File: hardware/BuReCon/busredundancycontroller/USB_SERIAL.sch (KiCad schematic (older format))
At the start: 27 parts, among them U4 FT2232HL, U5 USBLC6-2SC6, U6 93LC56C, U7 DSC1001DI1

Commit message: House Keeping
House keeping
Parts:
- C13, C14, C15, C16, C17, C18, C19, C20, C21, C22, C23, C24, C25, C26, C27: footprint (none) -> Capacitor_SMD:C_0201_0603Metric
- FB2, FB3: footprint (none) -> Fuse:Fuse_0603_1608Metric
- R2, R3, R4, R5, R6, R7: footprint (none) -> Resistor_SMD:R_0603_1608Metric
- U6: footprint (none) -> Package_TO_SOT_SMD:SOT-23-8
- U7: footprint CDFN4_2P5X2_MCH -> CDFN4_2P5X2_MCH:DSC1001DI1-033.3333T
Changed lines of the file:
@@
 F 0 "C16" H 9042 1846 50  0000 L CNN
 F 1 "100nF" H 9042 1755 50  0000 L CNN
-F 2 "" H 8950 1800 50  0001 C CNN
+F 2 "Capacitor_SMD:C_0201_0603Metric" H 8950 1800 50  0001 C CNN
 F 3 "~" H 8950 1800 50  0001 C CNN
 	1    8950 1800
@@
 F 0 "C17" H 9442 1846 50  0000 L CNN
 F 1 "100nF" H 9442 1755 50  0000 L CNN
-F 2 "" H 9350 1800 50  0001 C CNN
+F 2 "Capacitor_SMD:C_0201_0603Metric" H 9350 1800 50  0001 C CNN
 F 3 "~" H 9350 1800 50  0001 C CNN
 	1    9350 1800
@@
 F 0 "C18" H 9842 1846 50  0000 L CNN
 F 1 "100nF" H 9842 1755 50  0000 L CNN
-F 2 "" H 9750 1800 50  0001 C CNN
+F 2 "Capacitor_SMD:C_0201_0603Metric" H 9750 1800 50  0001 C CNN
 F 3 "~" H 9750 1800 50  0001 C CNN
 	1    9750 1800
@@
 F 0 "C15" H 8642 1846 50  0000 L CNN
 F 1 "100nF" H 8642 1755 50  0000 L CNN
-F 2 "" H 8550 1800 50  0001 C CNN
+F 2 "Capacitor_SMD:C_0201_0603Metric" H 8550 1800 50  0001 C CNN
 F 3 "~" H 8550 1800 50  0001 C CNN
 	1    8550 1800
@@
 F 0 "FB2" V 4400 950 50  0000 C CNN
 F 1 "BLM18SG121TN1D" V 4700 900 50  0000 C CNN
-F 2 "" V 4480 950 50  0001 C CNN
+F 2 "Fuse:Fuse_0603_1608Metric" V 4480 950 50  0001 C CNN
 F 3 "https://datasheet.octopart.com/BLM18SG121TN1D-Murata-datasheet-138707216.pdf" H 4550 950 50  0001 C CNN
 	1    4550 950
@@
 F 0 "FB3" V 3900 1650 50  0000 C CNN
 F 1 "BLM18SG121TN1D" V 4200 1450 50  0000 C CNN
-F 2 "" V 3980 1650 50  0001 C CNN
+F 2 "Fuse:Fuse_0603_1608Metric" V 3980 1650 50  0001 C CNN
 F 3 "https://datasheet.octopart.com/BLM18SG121TN1D-Murata-datasheet-138707216.pdf" H 4050 1650 50  0001 C CNN
 	1    4050 1650
@@
 F 0 "C13" H 5092 1146 50  0000 L CNN
 F 1 "10nF" H 5092 1055 50  0000 L CNN
-F 2 "" H 5000 1100 50  0001 C CNN
+F 2 "Capacitor_SMD:C_0201_0603Metric" H 5000 1100 50  0001 C CNN
 F 3 "~" H 5000 1100 50  0001 C CNN
 	1    5000 1100
@@
 F 0 "C14" H 5492 1146 50  0000 L CNN
 F 1 "100nF" H 5492 1055 50  0000 L CNN
-F 2 "" H 5400 1100 50  0001 C CNN
+F 2 "Capacitor_SMD:C_0201_0603Metric" H 5400 1100 50  0001 C CNN
 F 3 "~" H 5400 1100 50  0001 C CNN
 	1    5400 1100
@@
 F 0 "C19" H 4392 1796 50  0000 L CNN
 F 1 "10nF" H 4392 1705 50  0000 L CNN
-F 2 "" H 4300 1750 50  0001 C CNN
+F 2 "Capacitor_SMD:C_0201_0603Metric" H 4300 1750 50  0001 C CNN
 F 3 "~" H 4300 1750 50  0001 C CNN
 	1    4300 1750
@@
 F 0 "C20" H 4842 1796 50  0000 L CNN
 F 1 "100nF" H 4842 1705 50  0000 L CNN
-F 2 "" H 4750 1750 50  0001 C CNN
+F 2 "Capacitor_SMD:C_0201_0603Metric" H 4750 1750 50  0001 C CNN
 F 3 "~" H 4750 1750 50  0001 C CNN
 	1    4750 1750
@@
 F 0 "C21" H 3592 2346 50  0000 L CNN
 F 1 "100nF" H 3592 2255 50  0000 L CNN
-F 2 "" H 3500 2300 50  0001 C CNN
+F 2 "Capacitor_SMD:C_0201_0603Metric" H 3500 2300 50  0001 C CNN
 F 3 "~" H 3500 2300 50  0001 C CNN
 	1    3500 2300
@@
 F 0 "U7" H 3300 6400 60  0000 C CNN
 F 1 "DSC1001DI1" H 3150 5500 60  0000 C CNN
-F 2 "CDFN4_2P5X2_MCH" H 2800 6390 60  0001 C CNN
+F 2 "CDFN4_2P5X2_MCH:DSC1001DI1-033.3333T" H 2800 6390 60  0001 C CNN
 F 3 "" H 1900 6150 60  0000 C CNN
 	1    1900 6150
@@
 F 0 "C27" V 1550 6250 50  0000 L CNN
 F 1 "100nF" V 1750 6150 50  0000 L CNN
-F 2 "" H 1650 6350 50  0001 C CNN
+F 2 "Capacitor_SMD:C_0201_0603Metric" H 1650 6350 50  0001 C CNN
 F 3 "~" H 1650 6350 50  0001 C CNN
 	1    1650 6350
@@
 F 0 "R2" V 3900 3600 50  0000 C CNN
 F 1 "1k 5%" V 4100 3600 50  0000 C CNN
-F 2 "" H 4000 3600 50  0001 C CNN
+F 2 "Resistor_SMD:R_0603_1608Metric" H 4000 3600 50  0001 C CNN
 F 3 "~" H 4000 3600 50  0001 C CNN
 	1    4000 3600
@@
 F 0 "R3" V 4400 3800 50  0000 C CNN
 F 1 "12k 5%" V 4600 3800 50  0000 C CNN
-F 2 "" H 4500 3800 50  0001 C CNN
+F 2 "Resistor_SMD:R_0603_1608Metric" H 4500 3800 50  0001 C CNN
 F 3 "~" H 4500 3800 50  0001 C CNN
 	1    4500 3800
@@
 F 0 "U6" H 2050 4950 50  0000 C CNN
 F 1 "93LC56C" H 2200 4450 50  0000 C CNN
-F 2 "" H 1950 4700 50  0001 C CNN
+F 2 "Package_TO_SOT_SMD:SOT-23-8" H 1950 4700 50  0001 C CNN
 F 3 "http://ww1.microchip.com/downloads/en/DeviceDoc/20001749K.pdf" H 1950 4700 50  0001 C CNN
 	1    1950 4700
@@
 F 0 "C26" H 1242 5046 50  0000 L CNN
 F 1 "100nF" H 1242 4955 50  0000 L CNN
-F 2 "" H 1150 5000 50  0001 C CNN
+F 2 "Capacitor_SMD:C_0201_0603Metric" H 1150 5000 50  0001 C CNN
 F 3 "~" H 1150 5000 50  0001 C CNN
 	1    1150 5000
@@
 F 0 "R4" H 1509 4396 50  0000 L CNN
 F 1 "10k 1%" H 1509 4305 50  0000 L CNN
-F 2 "" H 1450 4350 50  0001 C CNN
+F 2 "Resistor_SMD:R_0603_1608Metric" H 1450 4350 50  0001 C CNN
 F 3 "~" H 1450 4350 50  0001 C CNN
 	1    1450 4350
@@
 F 0 "R7" V 2750 4700 50  0000 C CNN
 F 1 "2k2 5%" V 2750 4900 50  0000 C CNN
-F 2 "" H 2650 4800 50  0001 C CNN
+F 2 "Resistor_SMD:R_0603_1608Metric" H 2650 4800 50  0001 C CNN
 F 3 "~" H 2650 4800 50  0001 C CNN
 	1    2650 4800
@@
 F 0 "R6" H 2859 4446 50  0000 L CNN
 F 1 "10k 1%" H 2859 4355 50  0000 L CNN
-F 2 "" H 2800 4400 50  0001 C CNN
+F 2 "Resistor_SMD:R_0603_1608Metric" H 2800 4400 50  0001 C CNN
 F 3 "~" H 2800 4400 50  0001 C CNN
 	1    2800 4400
@@
 F 0 "R5" H 2500 4450 50  0000 L CNN
 F 1 "10k 1%" H 2300 4350 50  0000 L CNN
-F 2 "" H 2650 4400 50  0001 C CNN
+F 2 "Resistor_SMD:R_0603_1608Metric" H 2650 4400 50  0001 C CNN
 F 3 "~" H 2650 4400 50  0001 C CNN
 	1    2650 4400
@@
 F 0 "C22" H 6392 996 50  0000 L CNN
 F 1 "100nF" H 6392 905 50  0000 L CNN
-F 2 "" H 6300 950 50  0001 C CNN
+F 2 "Capacitor_SMD:C_0201_0603Metric" H 6300 950 50  0001 C CNN
 F 3 "~" H 6300 950 50  0001 C CNN
 	1    6300 950
@@
 F 0 "C23" H 6792 996 50  0000 L CNN
 F 1 "100nF" H 6792 905 50  0000 L CNN
-F 2 "" H 6700 950 50  0001 C CNN
+F 2 "Capacitor_SMD:C_0201_0603Metric" H 6700 950 50  0001 C CNN
 F 3 "~" H 6700 950 50  0001 C CNN
 	1    6700 950
@@
 F 0 "C24" H 7192 996 50  0000 L CNN
 F 1 "100nF" H 7192 905 50  0000 L CNN
-F 2 "" H 7100 950 50  0001 C CNN
+F 2 "Capacitor_SMD:C_0201_0603Metric" H 7100 950 50  0001 C CNN
 F 3 "~" H 7100 950 50  0001 C CNN
 	1    7100 950
@@
 F 0 "C25" H 4442 2646 50  0000 L CNN
 F 1 "10nF" H 4442 2555 50  0000 L CNN
-F 2 "" H 4350 2600 50  0001 C CNN
+F 2 "Capacitor_SMD:C_0201_0603Metric" H 4350 2600 50  0001 C CNN
 F 3 "~" H 4350 2600 50  0001 C CNN
 	1    4350 2600

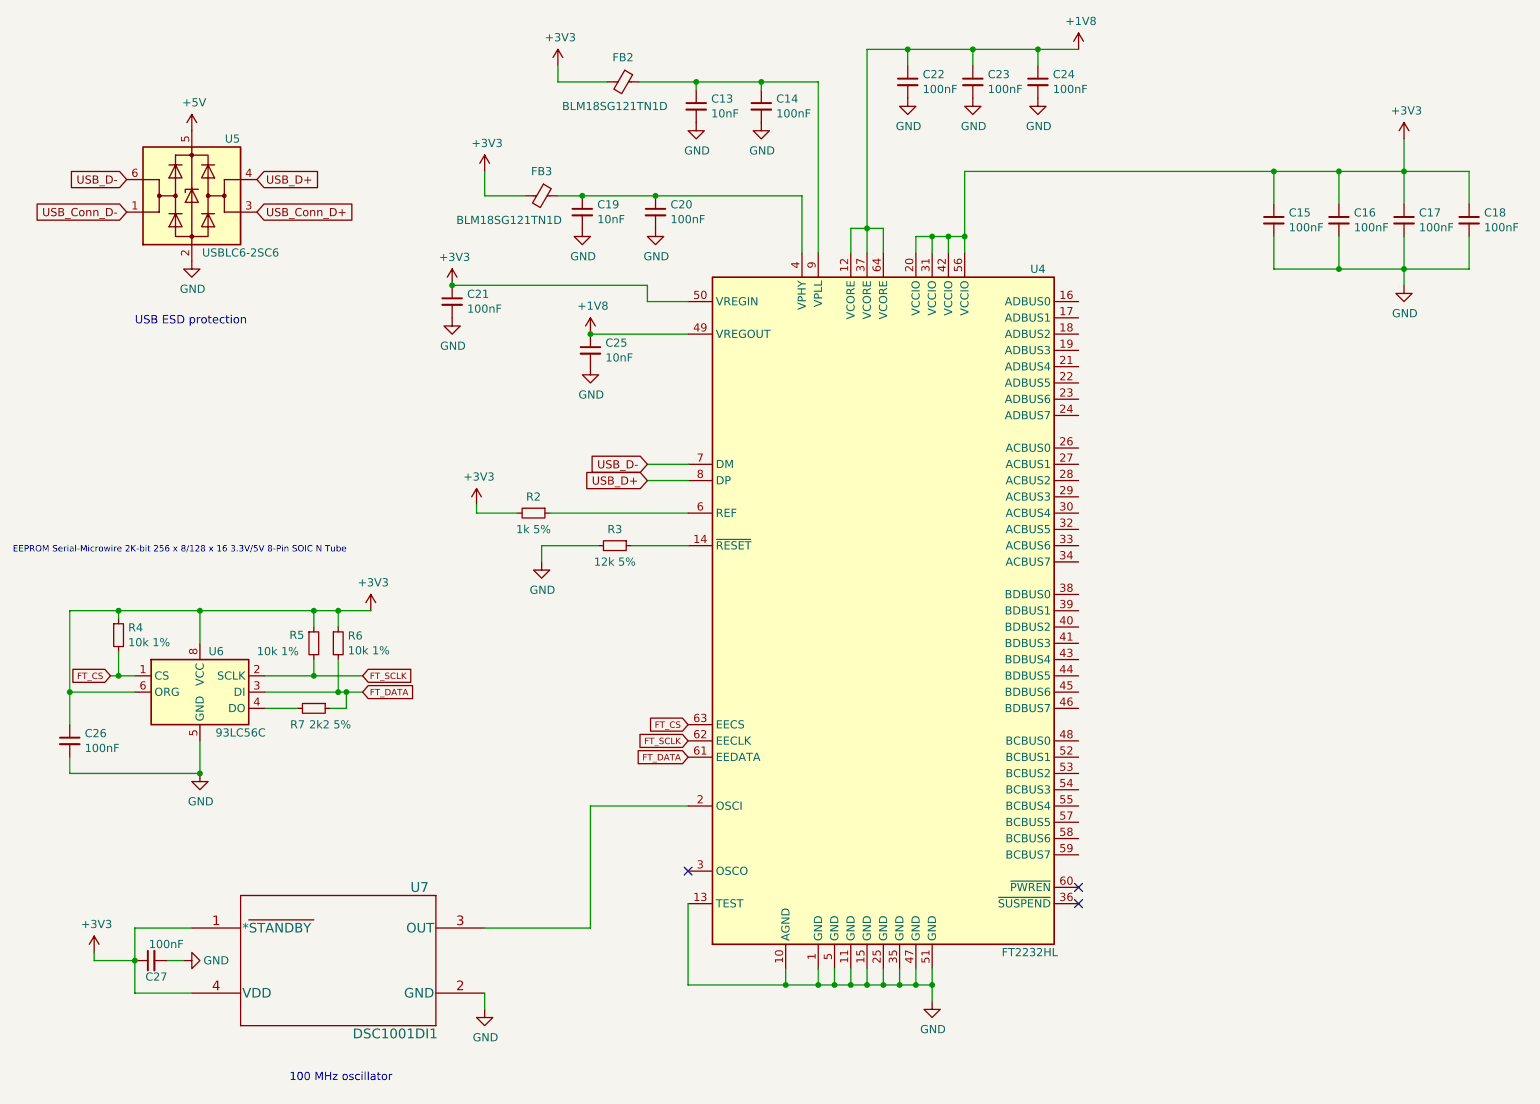
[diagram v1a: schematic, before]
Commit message: FPGA configuration
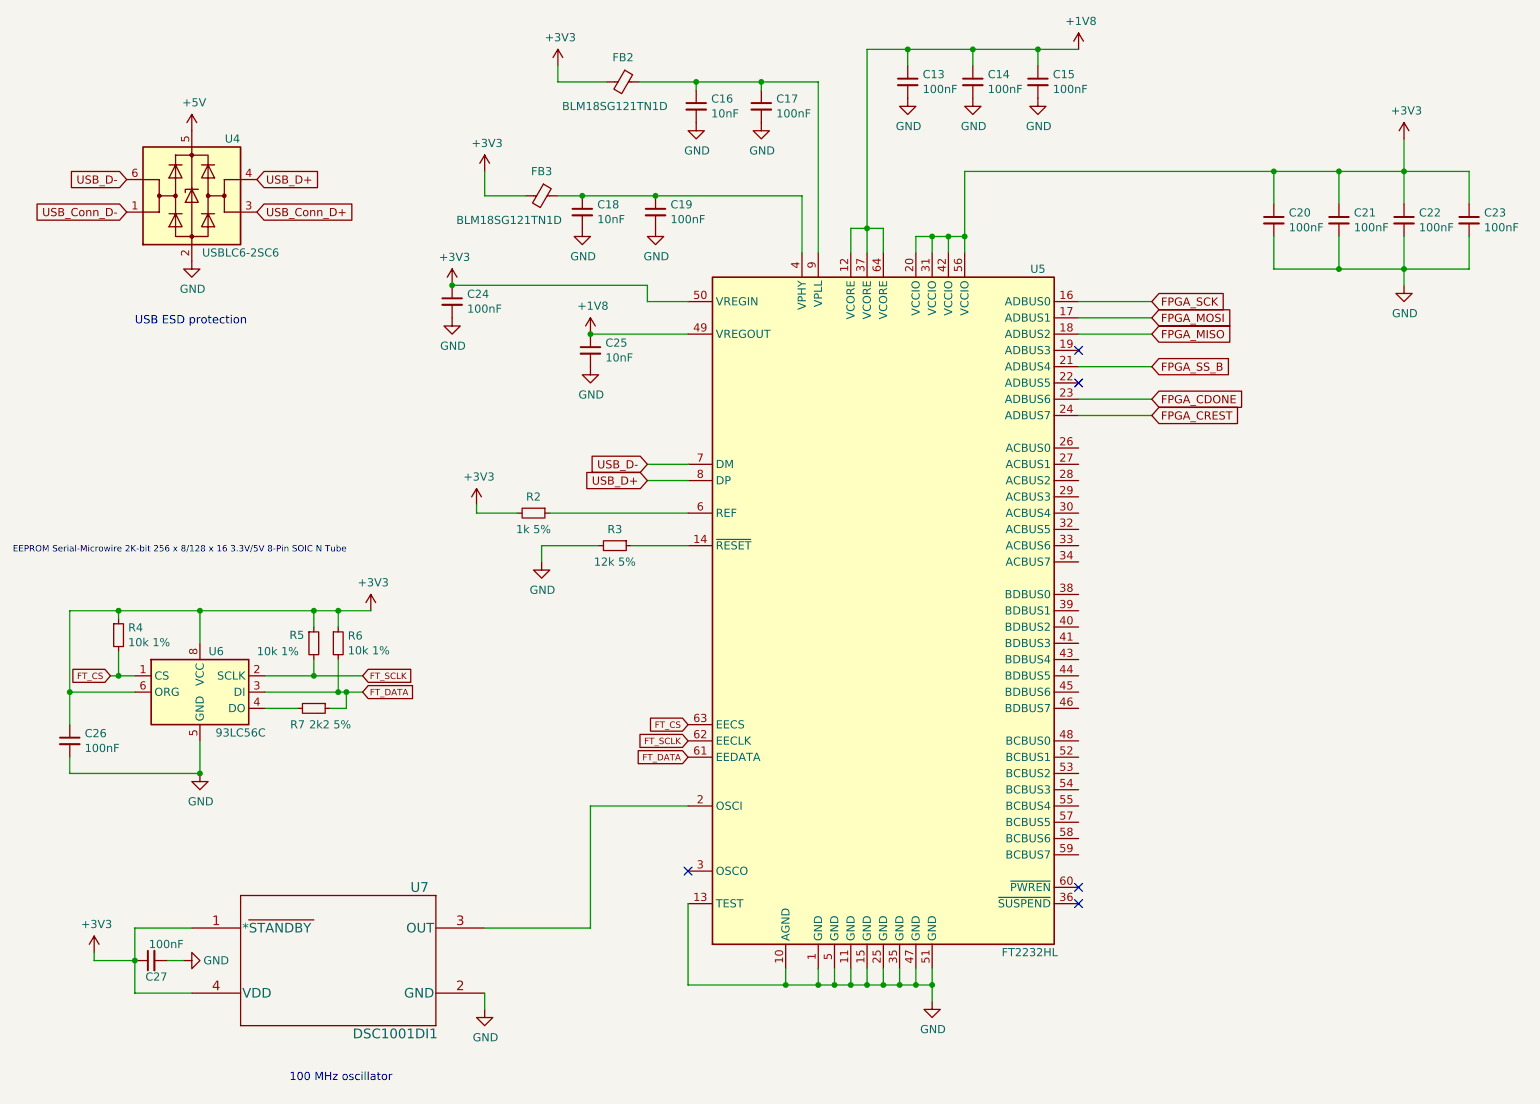
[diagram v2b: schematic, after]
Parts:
- renumbered C22 to C13, C23 to C14, C24 to C15, C13 to C16, C14 to C17, C19 to C18, C20 to C19, C15 to C20, C16 to C21, C17 to C22, C18 to C23, C21 to C24, U5 to U4, U4 to U5
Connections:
- net FPGA_SCK: now reaches U5.16 (ADBUS0)
- net FPGA_MOSI: now reaches U5.17 (ADBUS1)
- net FPGA_MISO: now reaches U5.18 (ADBUS2)
- net FPGA_SS_B: now reaches U5.21 (ADBUS4)
- net FPGA_CDONE: now reaches U5.23 (ADBUS6)
- net FPGA_CREST: now reaches U5.24 (ADBUS7)
- no-connect marks 3 -> 5

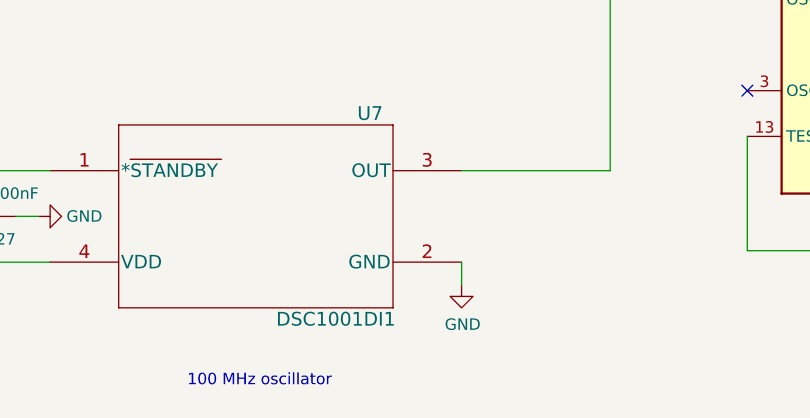
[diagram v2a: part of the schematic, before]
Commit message: Cleanup and IO banks
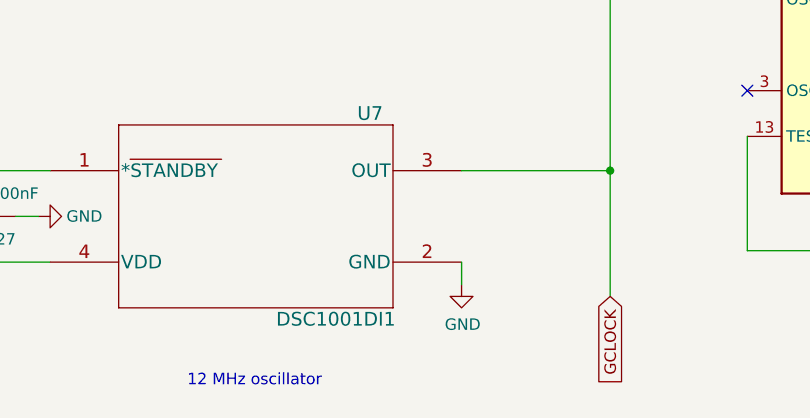
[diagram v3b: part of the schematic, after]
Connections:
- net GCLOCK: now reaches U5.2 (OSCI), U7.3 (OUT)
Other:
- note added: "12 MHz oscillator"
- note removed: "100 MHz oscillator"
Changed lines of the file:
@@
 encoding utf-8
 Sheet 3 5
-Title ""
+Title "USB & Serial"
 Date ""
 Rev ""
@@
 $EndComp
 Text Notes 2500 7100 0    50   ~ 0
-100 MHz oscillator
+12 MHz oscillator
 $Comp
 L power:GND #PWR051
@@
 Text GLabel 7800 2300 2    50   Input ~ 0
 FPGA_SCK
+Text GLabel 4350 6700 3    50   Input ~ 0
+GCLOCK
+Wire Wire Line
+	4350 6700 4350 6150
+Connection ~ 4350 6150
 $EndSCHEMATC

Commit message: Connectors and RS232
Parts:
- added LD3: Yellow, LED_SMD:LED_0201_0603Metric, symbol Device:LED_ALT
- added LD4: Green, LED_SMD:LED_0201_0603Metric, symbol Device:LED_ALT
- added R19, R22: 100R, Resistor_SMD:R_0603_1608Metric, symbol Device:R_Small
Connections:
- net +3V3: now also LD3.2 (A), LD4.2 (A)
- net FT_TXD: now reaches U5.38 (BDBUS0)
- net FT_RXD: now reaches U5.39 (BDBUS1)
- net at U5.54 (BCBUS3): now also R19.2
- net at U5.55 (BCBUS4): now also R22.2
- new net: LD3.1 (K), R19.1
- new net: LD4.1 (K), R22.1
- no-connect marks 5 -> 25
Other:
- note added: "FPGA Rx"
- note added: "FPGA Tx"
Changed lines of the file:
@@
 	1    0    0    -1
 $EndComp
-Text Notes 2500 7100 0    50   ~ 0
+Text Notes 2500 7000 0    50   ~ 0
 12 MHz oscillator
 $Comp
@@
 	4350 6700 4350 6150
 Connection ~ 4350 6150
+Text GLabel 7850 4200 2    50   Input ~ 0
+FT_RXD
+Wire Wire Line
+	7350 4200 7850 4200
+$Comp
+L Device:LED_ALT LD?
+U 1 1 5F8D7099
+P 8700 5150
+AR Path="/5F7B6286/5F8D7099" Ref="LD?"  Part="1"
+AR Path="/5F7E5564/5F8D7099" Ref="LD3"  Part="1"
+F 0 "LD3" H 8850 5250 50  0000 R CNN
+F 1 "Yellow" H 8850 5050 50  0000 R CNN
+F 2 "LED_SMD:LED_0201_0603Metric" H 8700 5150 50  0001 C CNN
+F 3 "~" H 8700 5150 50  0001 C CNN
+	1    8700 5150
+	1    0    0    -1
+$EndComp
+$Comp
+L Device:R_Small R19
+U 1 1 5F8E6A23
+P 8200 5150
+F 0 "R19" V 8100 5150 50  0000 L CNN
+F 1 "100R" V 8300 5100 50  0000 L CNN
+F 2 "Resistor_SMD:R_0603_1608Metric" H 8200 5150 50  0001 C CNN
+F 3 "~" H 8200 5150 50  0001 C CNN
+	1    8200 5150
+	0    1    1    0
+$EndComp
+Wire Wire Line
+	8300 5150 8550 5150
+Wire Wire Line
+	8100 5150 7550 5150
+$Comp
+L power:+3V3 #PWR?
+U 1 1 5F8F87FC
+P 9050 4850
+AR Path="/5F7B6286/5F8F87FC" Ref="#PWR?"  Part="1"
+AR Path="/5F7E5564/5F8F87FC" Ref="#PWR058"  Part="1"
+F 0 "#PWR058" H 9050 4700 50  0001 C CNN
+F 1 "+3V3" H 9065 5023 50  0000 C CNN
+F 2 "" H 9050 4850 50  0001 C CNN
+F 3 "" H 9050 4850 50  0001 C CNN
+	1    9050 4850
+	1    0    0    -1
+$EndComp
+Wire Wire Line
+	8850 5150 9050 5150
+Wire Wire Line
+	9050 5150 9050 4850
+Text Notes 8550 5000 0    50   ~ 0
+FPGA Tx
+NoConn ~ 7350 3200
+NoConn ~ 7350 3300
+NoConn ~ 7350 3400
+NoConn ~ 7350 3500
+NoConn ~ 7350 3600
+NoConn ~ 7350 3700
+NoConn ~ 7350 3800
+NoConn ~ 7350 3900
+NoConn ~ 7350 4300
+NoConn ~ 7350 4400
+NoConn ~ 7350 4500
+NoConn ~ 7350 4600
+NoConn ~ 7350 4700
+NoConn ~ 7350 4800
+NoConn ~ 7350 5000
+NoConn ~ 7350 5100
+NoConn ~ 7350 5200
+NoConn ~ 7350 5500
+NoConn ~ 7350 5600
+NoConn ~ 7350 5700
+Text GLabel 7850 4100 2    50   Input ~ 0
+FT_TXD
+Wire Wire Line
+	7850 4100 7350 4100
+$Comp
+L Device:LED_ALT LD?
+U 1 1 5F98A8DA
+P 9500 5450
+AR Path="/5F7B6286/5F98A8DA" Ref="LD?"  Part="1"
+AR Path="/5F7E5564/5F98A8DA" Ref="LD4"  Part="1"
+F 0 "LD4" H 9650 5550 50  0000 R CNN
+F 1 "Green" H 9650 5350 50  0000 R CNN
+F 2 "LED_SMD:LED_0201_0603Metric" H 9500 5450 50  0001 C CNN
+F 3 "~" H 9500 5450 50  0001 C CNN
+	1    9500 5450
+	1    0    0    -1
+$EndComp
+$Comp
+L Device:R_Small R22
+U 1 1 5F98A8E0
+P 9000 5450
+F 0 "R22" V 8900 5450 50  0000 L CNN
+F 1 "100R" V 9100 5400 50  0000 L CNN
+F 2 "Resistor_SMD:R_0603_1608Metric" H 9000 5450 50  0001 C CNN
+F 3 "~" H 9000 5450 50  0001 C CNN
+	1    9000 5450
+	0    1    1    0
+$EndComp
+Wire Wire Line
+	9100 5450 9350 5450
+Wire Wire Line
+	9650 5450 9850 5450
+Wire Wire Line
+	7550 5400 7550 5450
+Wire Wire Line
+	7550 5450 8900 5450
+Wire Wire Line
+	7350 5400 7550 5400
+$Comp
+L power:+3V3 #PWR?
+U 1 1 5F996D71
+P 9850 5000
+AR Path="/5F7B6286/5F996D71" Ref="#PWR?"  Part="1"
+AR Path="/5F7E5564/5F996D71" Ref="#PWR061"  Part="1"
+F 0 "#PWR061" H 9850 4850 50  0001 C CNN
+F 1 "+3V3" H 9865 5173 50  0000 C CNN
+F 2 "" H 9850 5000 50  0001 C CNN
+F 3 "" H 9850 5000 50  0001 C CNN
+	1    9850 5000
+	1    0    0    -1
+$EndComp
+Wire Wire Line
+	9850 5000 9850 5450
+Text Notes 9350 5300 0    50   ~ 0
+FPGA Rx
+Wire Wire Line
+	7550 5150 7550 5300
+Wire Wire Line
+	7550 5300 7350 5300
 $EndSCHEMATC
